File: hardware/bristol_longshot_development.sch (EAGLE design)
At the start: 107 parts, among them IC3 TLV70033DCK, U1 SAM_D20E, U2 SI4060, U3 MAX1947, U4 ANTENOVA_GPS_M10382, U5 S25FS-S, U6 STM32F_48PIN, U7 LP38501TS-ADJ/NOPB, Y1 8MHz

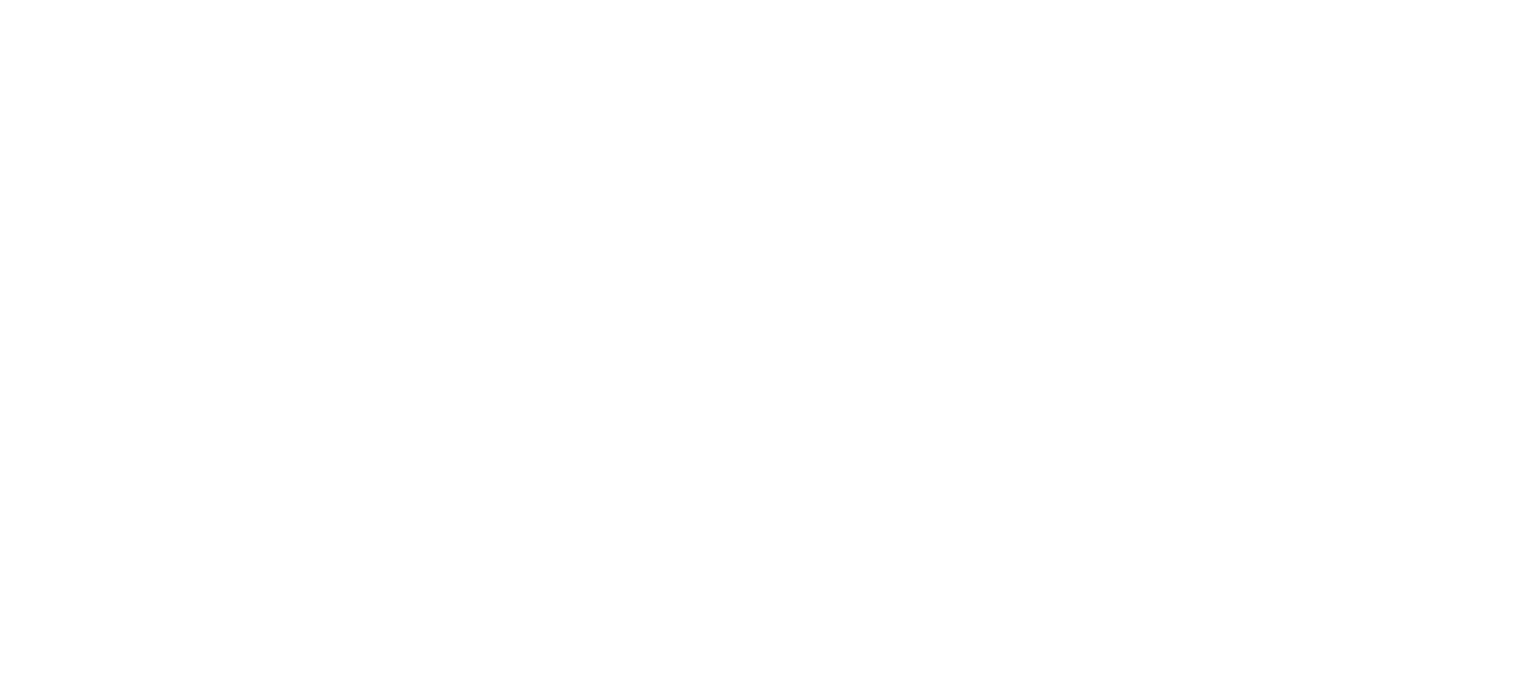
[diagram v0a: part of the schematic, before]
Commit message: Such commit. Many change.
GPS now seems to be alive on the dev board, using UBX mode. SAM D20 drivers coming along.

Timepulse next. And then radio
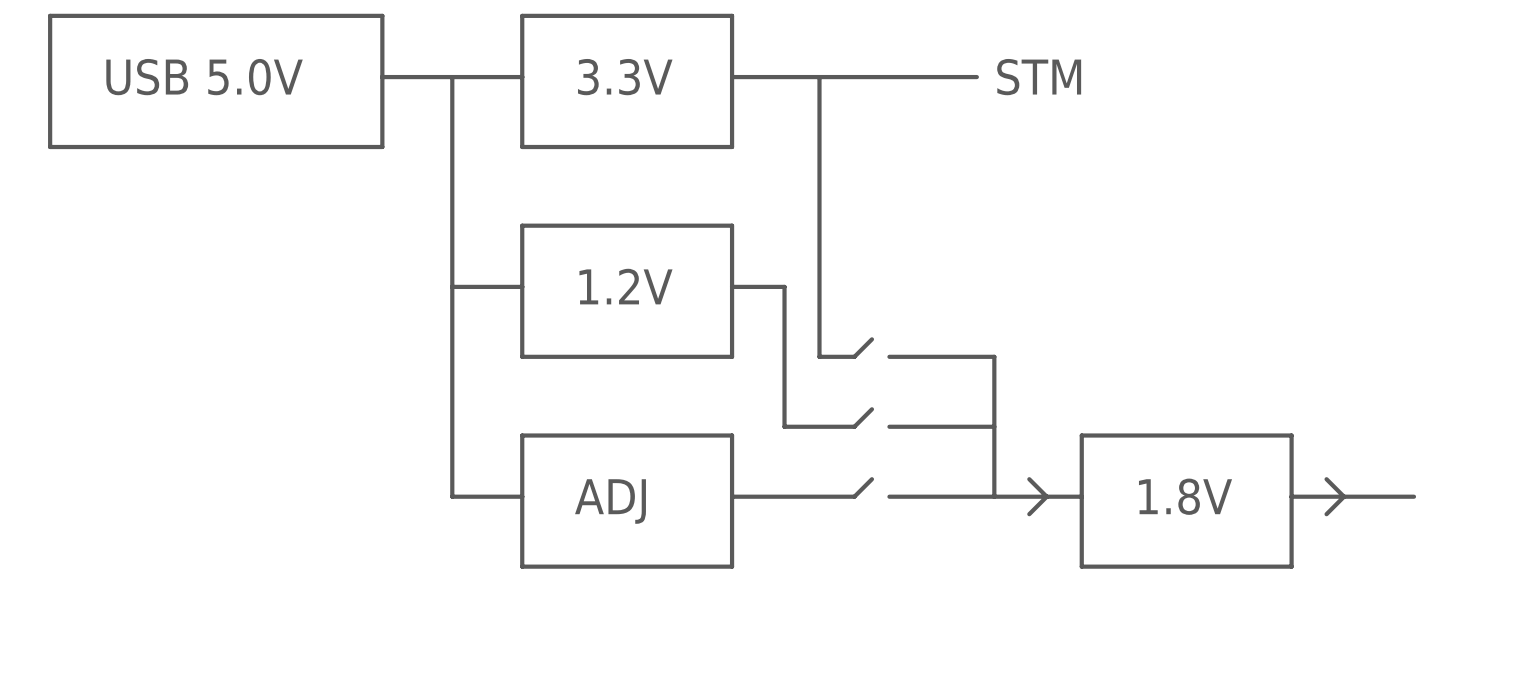
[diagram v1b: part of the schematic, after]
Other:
- note added: "1.2V"
- note added: "1.8V"
- note added: "3.3V"
- note added: "ADJ"
- note added: "STM"
- note added: "USB 5.0V"
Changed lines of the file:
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@@
 <part name="R22" library="microbuilder_v3" deviceset="RESISTOR" device="_0402" value="1Ω"/>
 <part name="R23" library="microbuilder_v3" deviceset="RESISTOR" device="_0402" value="1Ω"/>
+<part name="FRAME5" library="SparkFun" deviceset="FRAME-LETTER" device=""/>
 </parts>
 <sheets>
@@
 <text x="10.16" y="345.44" size="2.54" layer="97" font="vector" ratio="11">Busses</text>
 <text x="391.16" y="360.68" size="2.54" layer="97" font="vector" ratio="11">USB Interface</text>
+<wire x1="12.7" y1="542.29" x2="60.96" y2="542.29" width="0.6096" layer="97"/>
+<wire x1="60.96" y1="542.29" x2="60.96" y2="533.4" width="0.6096" layer="97"/>
+<wire x1="60.96" y1="533.4" x2="60.96" y2="523.24" width="0.6096" layer="97"/>
+<wire x1="60.96" y1="523.24" x2="12.7" y2="523.24" width="0.6096" layer="97"/>
+<wire x1="12.7" y1="523.24" x2="12.7" y2="542.29" width="0.6096" layer="97"/>
+<text x="20.32" y="530.86" size="5.08" layer="97" font="vector" ratio="11">USB 5.0V</text>
+<wire x1="81.28" y1="511.81" x2="111.76" y2="511.81" width="0.6096" layer="97"/>
+<wire x1="111.76" y1="511.81" x2="111.76" y2="502.92" width="0.6096" layer="97"/>
+<wire x1="111.76" y1="502.92" x2="111.76" y2="492.76" width="0.6096" layer="97"/>
+<wire x1="111.76" y1="492.76" x2="81.28" y2="492.76" width="0.6096" layer="97"/>
+<wire x1="81.28" y1="492.76" x2="81.28" y2="502.92" width="0.6096" layer="97"/>
+<text x="88.9" y="500.38" size="5.08" layer="97" font="vector" ratio="11">1.2V</text>
+<wire x1="81.28" y1="502.92" x2="81.28" y2="511.81" width="0.6096" layer="97"/>
+<wire x1="60.96" y1="533.4" x2="71.12" y2="533.4" width="0.6096" layer="97"/>
+<wire x1="71.12" y1="533.4" x2="71.12" y2="502.92" width="0.6096" layer="97"/>
+<wire x1="71.12" y1="502.92" x2="81.28" y2="502.92" width="0.6096" layer="97"/>
+<wire x1="81.28" y1="481.33" x2="111.76" y2="481.33" width="0.6096" layer="97"/>
+<wire x1="111.76" y1="481.33" x2="111.76" y2="472.44" width="0.6096" layer="97"/>
+<wire x1="111.76" y1="472.44" x2="111.76" y2="462.28" width="0.6096" layer="97"/>
+<wire x1="111.76" y1="462.28" x2="81.28" y2="462.28" width="0.6096" layer="97"/>
+<wire x1="81.28" y1="462.28" x2="81.28" y2="472.44" width="0.6096" layer="97"/>
+<text x="88.9" y="469.9" size="5.08" layer="97" font="vector" ratio="11">ADJ</text>
+<wire x1="81.28" y1="472.44" x2="81.28" y2="481.33" width="0.6096" layer="97"/>
+<wire x1="71.12" y1="502.92" x2="71.12" y2="472.44" width="0.6096" layer="97"/>
+<wire x1="71.12" y1="472.44" x2="81.28" y2="472.44" width="0.6096" layer="97"/>
+<wire x1="81.28" y1="542.29" x2="111.76" y2="542.29" width="0.6096" layer="97"/>
+<wire x1="111.76" y1="542.29" x2="111.76" y2="533.4" width="0.6096" layer="97"/>
+<wire x1="111.76" y1="533.4" x2="111.76" y2="523.24" width="0.6096" layer="97"/>
+<wire x1="111.76" y1="523.24" x2="81.28" y2="523.24" width="0.6096" layer="97"/>
+<wire x1="81.28" y1="523.24" x2="81.28" y2="533.4" width="0.6096" layer="97"/>
+<text x="88.9" y="530.86" size="5.08" layer="97" font="vector" ratio="11">3.3V</text>
+<wire x1="81.28" y1="533.4" x2="81.28" y2="542.29" width="0.6096" layer="97"/>
+<wire x1="71.12" y1="533.4" x2="81.28" y2="533.4" width="0.6096" layer="97"/>
+<wire x1="111.76" y1="533.4" x2="124.46" y2="533.4" width="0.6096" layer="97"/>
+<text x="149.86" y="530.86" size="5.08" layer="97" font="vector" ratio="11">STM</text>
+<wire x1="124.46" y1="533.4" x2="147.32" y2="533.4" width="0.6096" layer="97"/>
+<wire x1="111.76" y1="472.44" x2="129.54" y2="472.44" width="0.6096" layer="97"/>
+<wire x1="134.62" y1="472.44" x2="149.86" y2="472.44" width="0.6096" layer="97"/>
+<wire x1="129.54" y1="472.44" x2="132.08" y2="474.98" width="0.6096" layer="97"/>
+<wire x1="111.76" y1="502.92" x2="119.38" y2="502.92" width="0.6096" layer="97"/>
+<wire x1="119.38" y1="502.92" x2="119.38" y2="482.6" width="0.6096" layer="97"/>
+<wire x1="119.38" y1="482.6" x2="129.54" y2="482.6" width="0.6096" layer="97"/>
+<wire x1="129.54" y1="482.6" x2="132.08" y2="485.14" width="0.6096" layer="97"/>
+<wire x1="124.46" y1="533.4" x2="124.46" y2="492.76" width="0.6096" layer="97"/>
+<wire x1="124.46" y1="492.76" x2="129.54" y2="492.76" width="0.6096" layer="97"/>
+<wire x1="129.54" y1="492.76" x2="132.08" y2="495.3" width="0.6096" layer="97"/>
+<wire x1="134.62" y1="492.76" x2="149.86" y2="492.76" width="0.6096" layer="97"/>
+<wire x1="134.62" y1="482.6" x2="149.86" y2="482.6" width="0.6096" layer="97"/>
+<wire x1="149.86" y1="492.76" x2="149.86" y2="472.44" width="0.6096" layer="97"/>
+<wire x1="162.56" y1="481.33" x2="193.04" y2="481.33" width="0.6096" layer="97"/>
+<wire x1="193.04" y1="481.33" x2="193.04" y2="472.44" width="0.6096" layer="97"/>
+<wire x1="193.04" y1="472.44" x2="193.04" y2="462.28" width="0.6096" layer="97"/>
+<wire x1="193.04" y1="462.28" x2="162.56" y2="462.28" width="0.6096" layer="97"/>
+<wire x1="162.56" y1="462.28" x2="162.56" y2="472.44" width="0.6096" layer="97"/>
+<text x="170.18" y="469.9" size="5.08" layer="97" font="vector" ratio="11">1.8V</text>
+<wire x1="162.56" y1="472.44" x2="162.56" y2="481.33" width="0.6096" layer="97"/>
+<wire x1="149.86" y1="472.44" x2="157.48" y2="472.44" width="0.6096" layer="97"/>
+<wire x1="157.48" y1="472.44" x2="162.56" y2="472.44" width="0.6096" layer="97"/>
+<wire x1="193.04" y1="472.44" x2="200.66" y2="472.44" width="0.6096" layer="97"/>
+<wire x1="200.66" y1="472.44" x2="210.82" y2="472.44" width="0.6096" layer="97"/>
+<wire x1="157.48" y1="472.44" x2="154.94" y2="474.98" width="0.6096" layer="97"/>
+<wire x1="157.48" y1="472.44" x2="154.94" y2="469.9" width="0.6096" layer="97"/>
+<wire x1="200.66" y1="472.44" x2="198.12" y2="474.98" width="0.6096" layer="97"/>
+<wire x1="200.66" y1="472.44" x2="198.12" y2="469.9" width="0.6096" layer="97"/>
 </plain>
 <instances>
@@
 <instance part="R22" gate="G$1" x="91.44" y="215.9" rot="R90"/>
 <instance part="R23" gate="G$1" x="83.82" y="215.9" rot="R90"/>
+<instance part="FRAME5" gate="G$1" x="0" y="375.92"/>
+<instance part="FRAME5" gate="G$2" x="147.32" y="375.92"/>
 </instances>
 <busses>
